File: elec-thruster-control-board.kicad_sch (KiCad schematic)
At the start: 45 parts, among them J1 Conn_01x20_Socket, J10 Conn_01x02_Socket, J11 Conn_01x02_Socket, J13 Conn_02x05_Counter_Clockwise, J14 Conn_01x02_Socket, J2 Conn_01x02_Socket, J3 Conn_01x20_Socket, J4 Conn_01x02_Socket, J5 Conn_01x02_Socket, J6 Conn_01x02_Socket, J7 Conn_01x02_Socket, J8 Conn_01x02_Socket, J9 Conn_01x02_Socket

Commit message: Update 4:25 rewired to fit a pico footprint
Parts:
- removed J3: Conn_01x20_Socket, Connector_PinHeader_2.54mm:PinHeader_1x20_P2.54mm_Vertical_SMD_Pin1Left, symbol Connector:Conn_01x20_Socket
- added A1: RaspberryPi_Pico, Module:RaspberryPi_Pico_Common_THT, symbol MCU_Module:RaspberryPi_Pico
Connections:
- net GND: now reaches D1.1 (K), J2.1 (Pin_1), J4.1 (Pin_1)
- net GND: now also D11.1 (K), D12.1 (K), D13.1 (K), D14.1 (K), D15.1 (K), D16.1 (K), D2.1 (K), D3.1 (K), D4.1 (K), D5.1 (K), J14.1 (Pin_1), J5.1 (Pin_1), J6.1 (Pin_1)
- net at J4.2 (Pin_2): now also A1.4 (GPIO2)
- net at R16.2: now also A1.17 (GPIO13)
- net at R15.2: now also A1.16 (GPIO12)
- net at J2.2 (Pin_2): now also A1.1 (GPIO0)
- net at R3.2: now also A1.7 (GPIO5); no longer J13.3 (Pin_3)
- net at R1.2: now also A1.2 (GPIO1); no longer J13.1 (Pin_1)
- net at R2.2: now also A1.5 (GPIO3); no longer J13.2 (Pin_2)
- net at R4.2: now also A1.10 (GPIO7); no longer J13.4 (Pin_4)
- net at R5.2: now also A1.12 (GPIO9); no longer J13.5 (Pin_5)
- net at J6.2 (Pin_2): now also A1.11 (GPIO8)
- net at R13.2: now also A1.14 (GPIO10)
- net at R14.2: now also A1.15 (GPIO11)
- net at R12.2: now also A1.19 (GPIO14)
- net at R11.2: now also A1.20 (GPIO15)
- net at J5.2 (Pin_2): now also A1.6 (GPIO4)
- net at J14.2 (Pin_2): now also A1.9 (GPIO6)
- new net: A1.13 (GND), A1.18 (GND), A1.23 (GND), A1.28 (GND), A1.3 (GND), A1.38 (GND), A1.8 (GND)
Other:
- moved on the sheet: D10, D6, D7, D8, D9, J1, J10, J11, J7, J8, J9, R10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

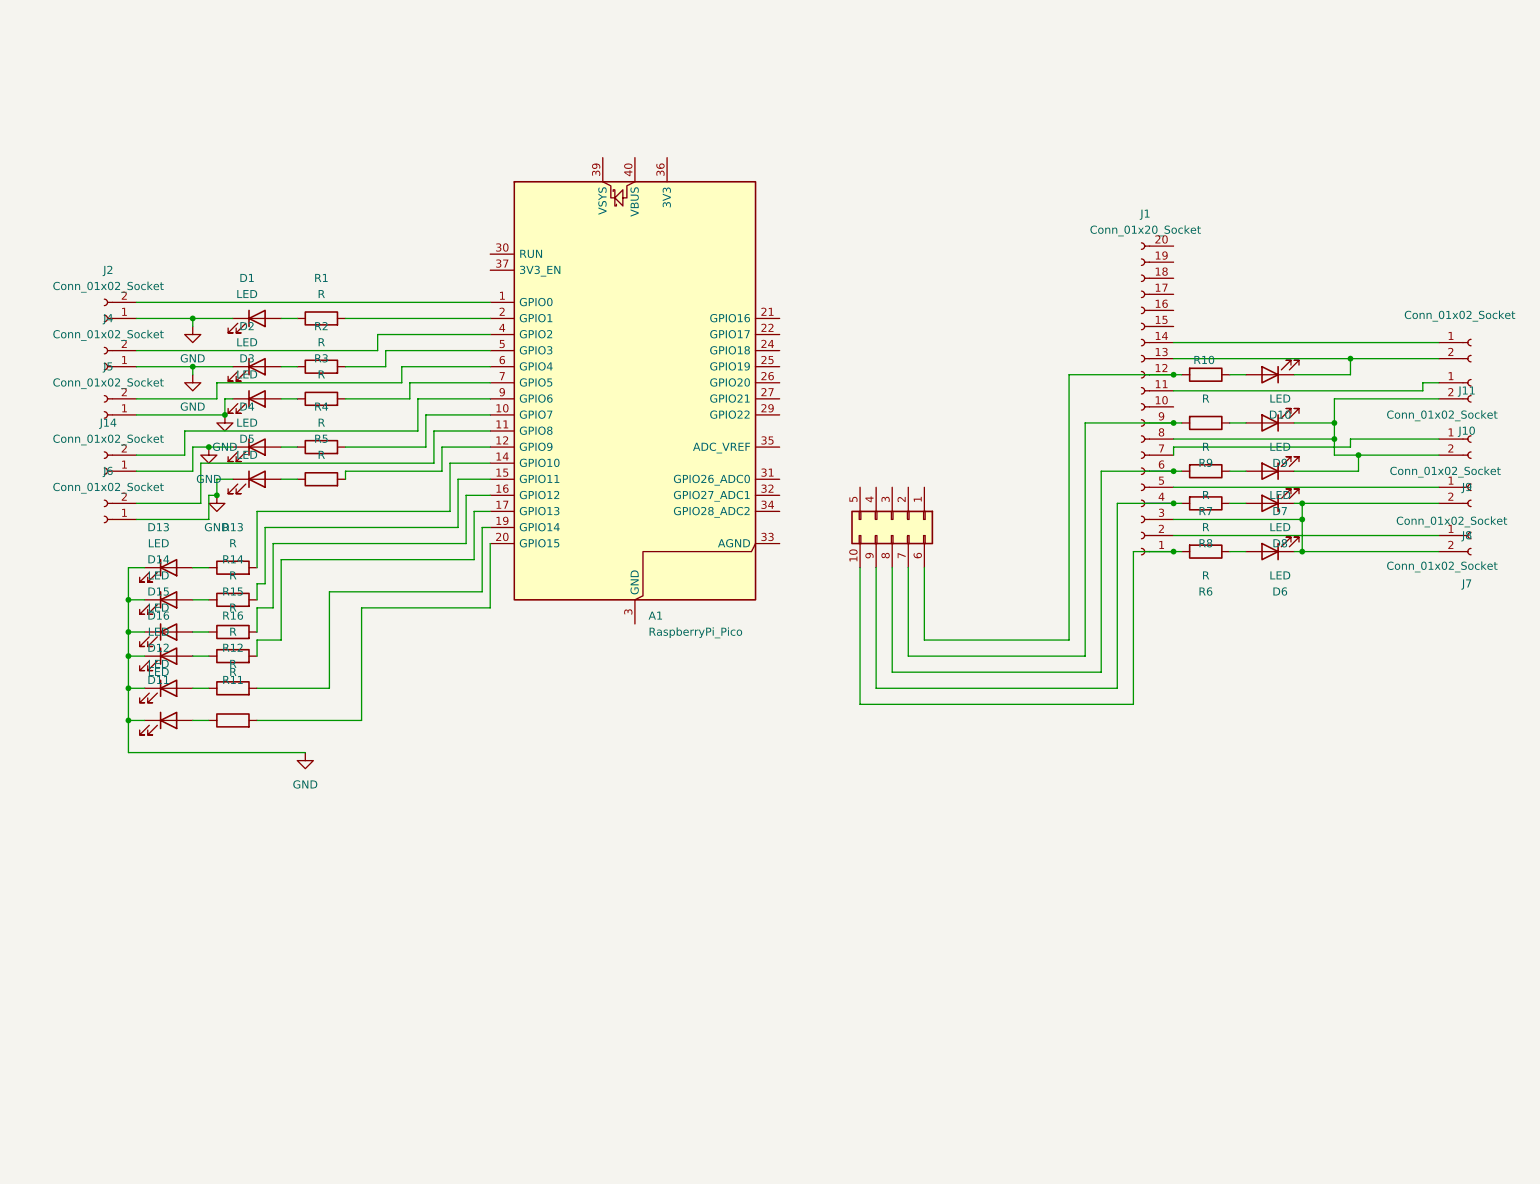
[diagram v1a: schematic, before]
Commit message: I fixed it such that the board now accurately fits a Pi Pico
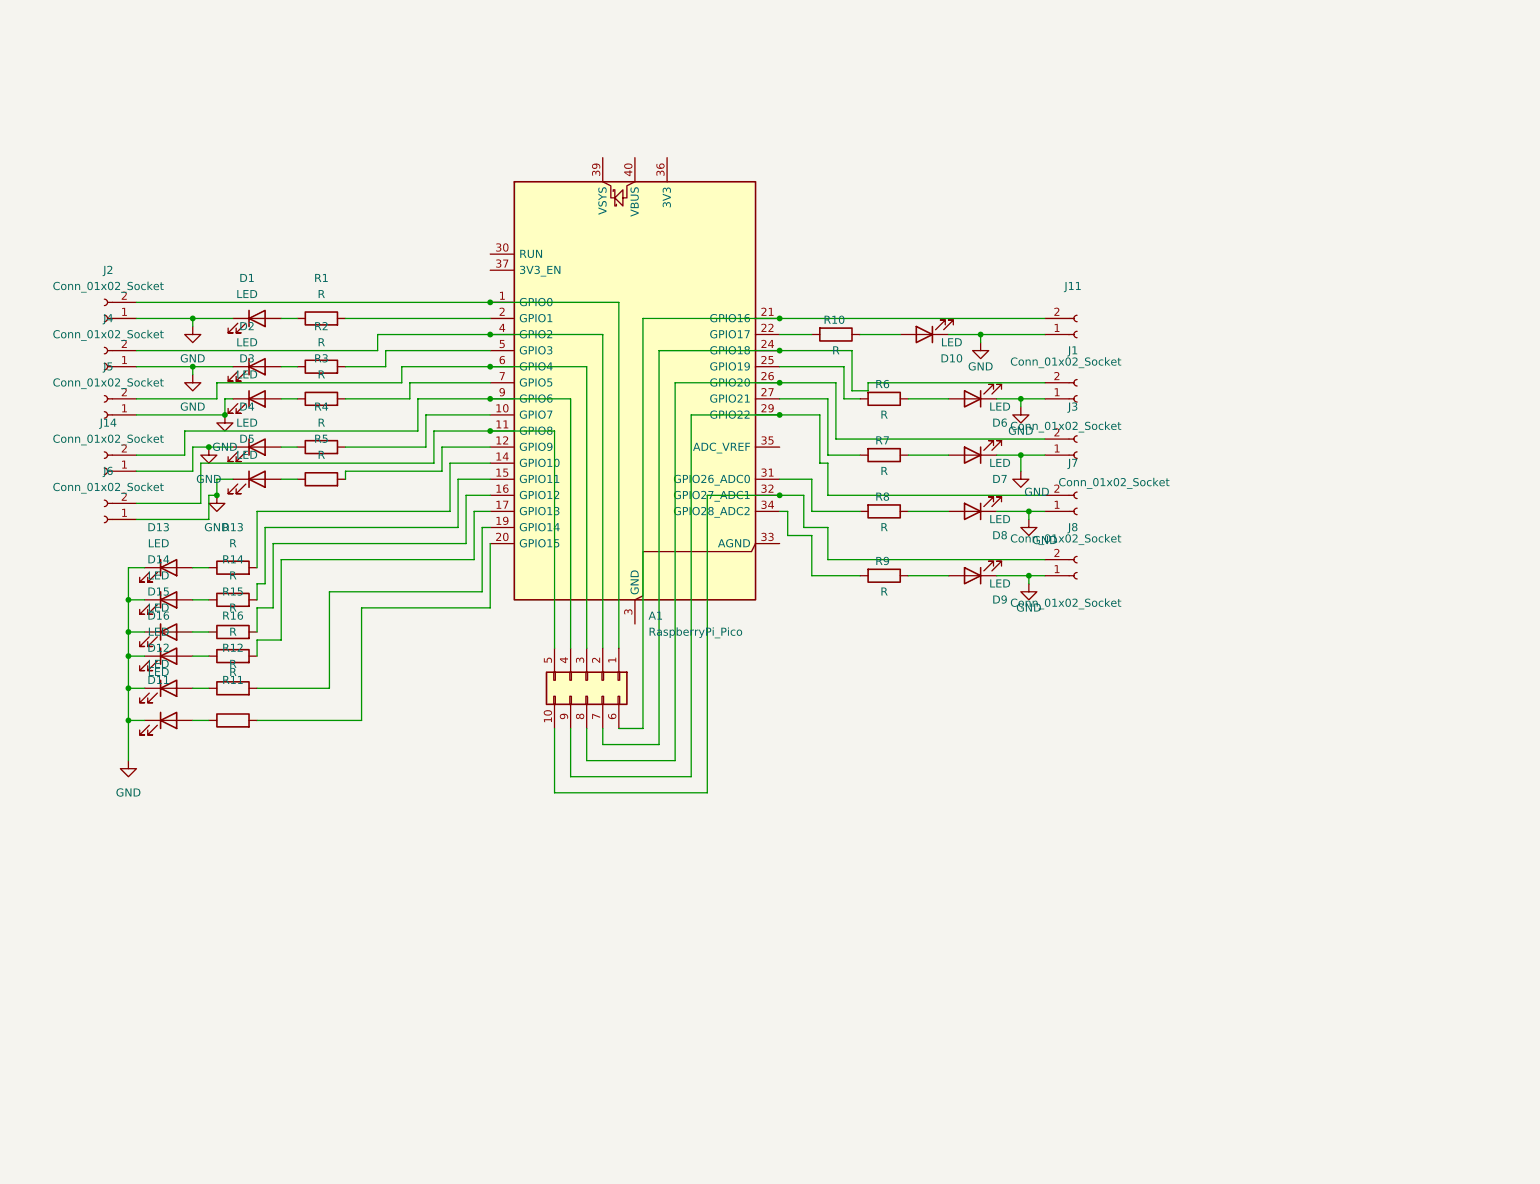
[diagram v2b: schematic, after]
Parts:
- removed J1: Conn_01x20_Socket, Connector_PinHeader_2.54mm:PinHeader_1x20_P2.54mm_Vertical_SMD_Pin1Right, symbol Connector:Conn_01x20_Socket
- removed J10, J9: Conn_01x02_Socket, Connector_JST:JST_GH_BM02B-GHS-TBT_1x02-1MP_P1.25mm_Vertical, symbol Connector:Conn_01x02_Socket
- added J1, J3: Conn_01x02_Socket, Connector_JST:JST_GH_BM02B-GHS-TBT_1x02-1MP_P1.25mm_Vertical, symbol Connector:Conn_01x02_Socket
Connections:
- net GND: now also D10.1 (K), D6.1 (K), D7.1 (K), D8.1 (K), D9.1 (K), J11.1 (Pin_1), J7.1 (Pin_1), J8.1 (Pin_1), J1.1 (Pin_1), J3.1 (Pin_1)
- net at A1.4 (GPIO2), J4.2 (Pin_2): now also J13.2 (Pin_2)
- net at J11.2 (Pin_2): now also A1.21 (GPIO16), J13.6 (Pin_10); no longer D10.1 (K)
- net at R10.2: now also A1.22 (GPIO17); no longer J13.6 (Pin_10)
- net at A1.1 (GPIO0), J2.2 (Pin_2): now also J13.1 (Pin_1)
- net at A1.11 (GPIO8), J6.2 (Pin_2): now also J13.5 (Pin_5)
- net at A1.24 (GPIO18): now also J13.7 (Pin_9), J1.2 (Pin_2)
- net at A1.25 (GPIO19): now also R6.2
- net at A1.26 (GPIO20): now also J13.8 (Pin_8), J3.2 (Pin_2)
- net at A1.27 (GPIO21): now also R7.2
- net at A1.29 (GPIO22): now also J13.9 (Pin_7), J7.2 (Pin_2)
- net at A1.31 (GPIO26_ADC0): now also R8.2
- net at A1.32 (GPIO27_ADC1): now also J13.10 (Pin_6), J8.2 (Pin_2)
- net at A1.34 (GPIO28_ADC2): now also R9.2
- net at A1.6 (GPIO4), J5.2 (Pin_2): now also J13.3 (Pin_3)
- net at A1.9 (GPIO6), J14.2 (Pin_2): now also J13.4 (Pin_4)
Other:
- moved on the sheet: D10, J11, R10

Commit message: needs work on the traces
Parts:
- J1, J11, J14, J2, J3, J4, J5, J6, J7, J8: symbol Connector:Conn_01x02_Socket -> Connector_Generic:Conn_01x02
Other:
- moved on the sheet: J1, J11, J14, J2, J3, J4, J5, J6, J7, J8
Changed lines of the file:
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@@
 	)
 	(symbol
-		(lib_id "Connector:Conn_01x02_Socket")
+		(lib_id "Connector_Generic:Conn_01x02")
 		(at 39.37 69.85 180)
 		(unit 1)
@@
 		(fields_autoplaced yes)
 		(property "Reference" "J4"
-			(at 40.005 62.23 0)
+			(at 39.37 60.96 0)
 			(effects
 				(font
@@
 		)
 		(property "Value" "Conn_01x02_Socket"
-			(at 40.005 64.77 0)
+			(at 39.37 63.5 0)
 			(effects
 				(font
@@
 			)
 		)
-		(property "Description" "Generic connector, single row, 01x02, script generated"
+		(property "Description" "Generic connector, single row, 01x02, script generated (kicad-library-utils/schlib/autogen/connector/)"
 			(at 39.37 69.85 0)
 			(effects
@@
 	)
 	(symbol
-		(lib_id "Connector:Conn_01x02_Socket")
+		(lib_id "Connector_Generic:Conn_01x02")
 		(at 193.04 64.77 0)
 		(mirror x)
@@
 			)
 		)
-		(property "Description" "Generic connector, single row, 01x02, script generated"
+		(property "Description" "Generic connector, single row, 01x02, script generated (kicad-library-utils/schlib/autogen/connector/)"
 			(at 193.04 64.77 0)
 			(effects
@@
 	)
 	(symbol
-		(lib_id "Connector:Conn_01x02_Socket")
+		(lib_id "Connector_Generic:Conn_01x02")
 		(at 39.37 62.23 180)
 		(unit 1)
@@
 		(fields_autoplaced yes)
 		(property "Reference" "J2"
-			(at 40.005 54.61 0)
+			(at 39.37 53.34 0)
 			(effects
 				(font
@@
 		)
 		(property "Value" "Conn_01x02_Socket"
-			(at 40.005 57.15 0)
+			(at 39.37 55.88 0)
 			(effects
 				(font
@@
 			)
 		)
-		(property "Description" "Generic connector, single row, 01x02, script generated"
+		(property "Description" "Generic connector, single row, 01x02, script generated (kicad-library-utils/schlib/autogen/connector/)"
 			(at 39.37 62.23 0)
 			(effects
@@
 	)
 	(symbol
-		(lib_id "Connector:Conn_01x02_Socket")
+		(lib_id "Connector_Generic:Conn_01x02")
 		(at 39.37 93.98 180)
 		(unit 1)
@@
 		(fields_autoplaced yes)
 		(property "Reference" "J6"
-			(at 40.005 86.36 0)
+			(at 39.37 85.09 0)
 			(effects
 				(font
@@
 		)
 		(property "Value" "Conn_01x02_Socket"
-			(at 40.005 88.9 0)
+			(at 39.37 87.63 0)
 			(effects
 				(font
@@
 			)
 		)
-		(property "Description" "Generic connector, single row, 01x02, script generated"
+		(property "Description" "Generic connector, single row, 01x02, script generated (kicad-library-utils/schlib/autogen/connector/)"
 			(at 39.37 93.98 0)
 			(effects
@@
 	)
 	(symbol
-		(lib_id "Connector:Conn_01x02_Socket")
+		(lib_id "Connector_Generic:Conn_01x02")
 		(at 39.37 77.47 180)
 		(unit 1)
@@
 		(fields_autoplaced yes)
 		(property "Reference" "J5"
-			(at 40.005 69.85 0)
+			(at 39.37 68.58 0)
 			(effects
 				(font
@@
 		)
 		(property "Value" "Conn_01x02_Socket"
-			(at 40.005 72.39 0)
+			(at 39.37 71.12 0)
 			(effects
 				(font
@@
 			)
 		)
-		(property "Description" "Generic connector, single row, 01x02, script generated"
+		(property "Description" "Generic connector, single row, 01x02, script generated (kicad-library-utils/schlib/autogen/connector/)"
 			(at 39.37 77.47 0)
 			(effects
@@
 	)
 	(symbol
-		(lib_id "Connector:Conn_01x02_Socket")
+		(lib_id "Connector_Generic:Conn_01x02")
 		(at 39.37 86.36 180)
 		(unit 1)
@@
 		(fields_autoplaced yes)
 		(property "Reference" "J14"
-			(at 40.005 78.74 0)
+			(at 39.37 77.47 0)
 			(effects
 				(font
@@
 		)
 		(property "Value" "Conn_01x02_Socket"
-			(at 40.005 81.28 0)
+			(at 39.37 80.01 0)
 			(effects
 				(font
@@
 			)
 		)
-		(property "Description" "Generic connector, single row, 01x02, script generated"
+		(property "Description" "Generic connector, single row, 01x02, script generated (kicad-library-utils/schlib/autogen/connector/)"
 			(at 39.37 86.36 0)
 			(effects
@@
 	)
 	(symbol
-		(lib_id "Connector:Conn_01x02_Socket")
+		(lib_id "Connector_Generic:Conn_01x02")
 		(at 193.04 83.82 0)
 		(mirror x)
@@
 			)
 		)
-		(property "Description" "Generic connector, single row, 01x02, script generated"
+		(property "Description" "Generic connector, single row, 01x02, script generated (kicad-library-utils/schlib/autogen/connector/)"
 			(at 193.04 83.82 0)
 			(effects
@@
 	)
 	(symbol
-		(lib_id "Connector:Conn_01x02_Socket")
+		(lib_id "Connector_Generic:Conn_01x02")
 		(at 193.04 74.93 0)
 		(mirror x)
@@
 			)
 		)
-		(property "Description" "Generic connector, single row, 01x02, script generated"
+		(property "Description" "Generic connector, single row, 01x02, script generated (kicad-library-utils/schlib/autogen/connector/)"
 			(at 193.04 74.93 0)
 			(effects
@@
 	)
 	(symbol
-		(lib_id "Connector:Conn_01x02_Socket")
+		(lib_id "Connector_Generic:Conn_01x02")
 		(at 193.04 102.87 0)
 		(mirror x)
@@
 			)
 		)
-		(property "Description" "Generic connector, single row, 01x02, script generated"
+		(property "Description" "Generic connector, single row, 01x02, script generated (kicad-library-utils/schlib/autogen/connector/)"
 			(at 193.04 102.87 0)
 			(effects
@@
 	)
 	(symbol
-		(lib_id "Connector:Conn_01x02_Socket")
+		(lib_id "Connector_Generic:Conn_01x02")
 		(at 193.04 92.71 0)
 		(mirror x)
@@
 			)
 		)
-		(property "Description" "Generic connector, single row, 01x02, script generated"
+		(property "Description" "Generic connector, single row, 01x02, script generated (kicad-library-utils/schlib/autogen/connector/)"
 			(at 193.04 92.71 0)
 			(effects
